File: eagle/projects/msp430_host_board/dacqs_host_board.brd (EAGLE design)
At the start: 127 x 100 mm, 272 parts, among them J1 MOL-SL-4-RA, J10 MOL-SL-3-V, J11 MOL-SL-2-V, J12 CONN HEADER 20POS .100" DBL, J13 MOL-SL-2-RA, J14 USB_MICROB_RECPT, J16 MOL-SL-2-RA, J17 CLM-112-02-L-D-IMU-MOUNT_IMU, J18 MOLSL-7-RA, J19 CONN HEADER 20POS .100" DBL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

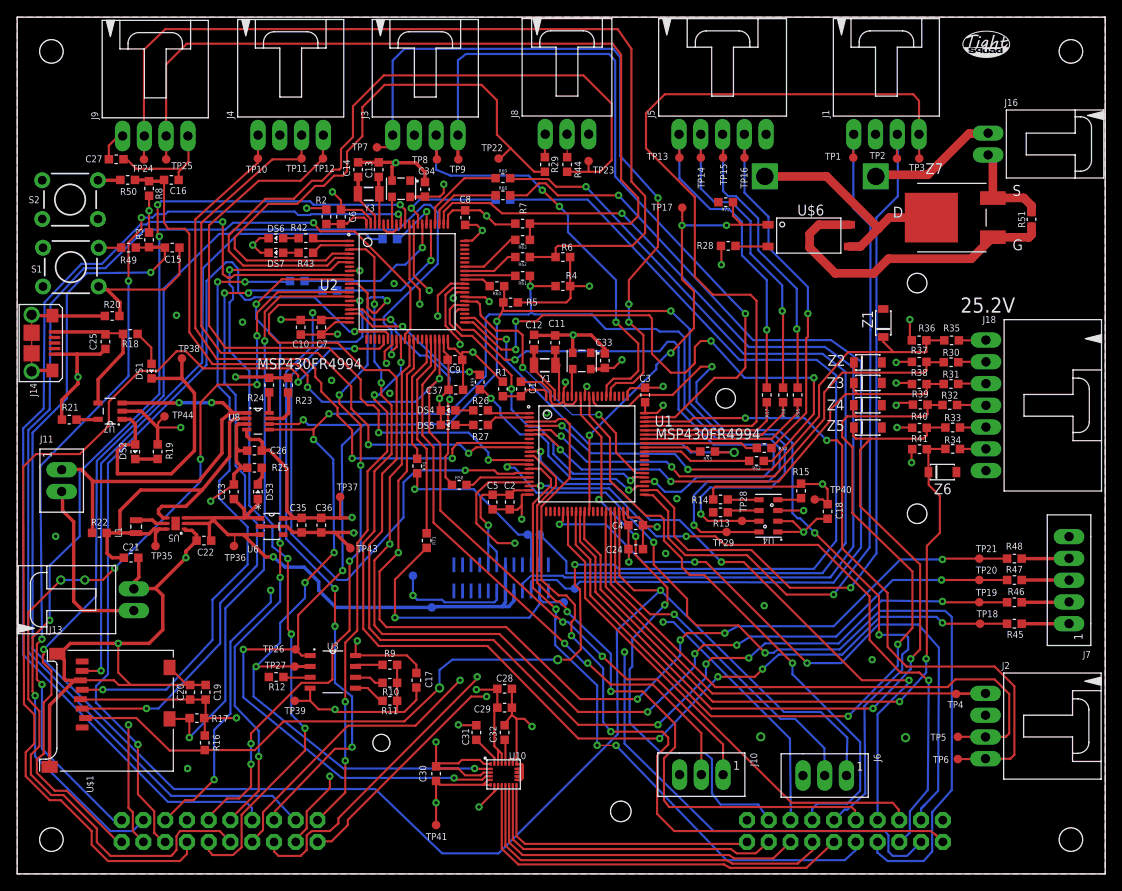
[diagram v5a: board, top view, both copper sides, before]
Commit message: Removed a large trace on power plane, updated some silkscreen
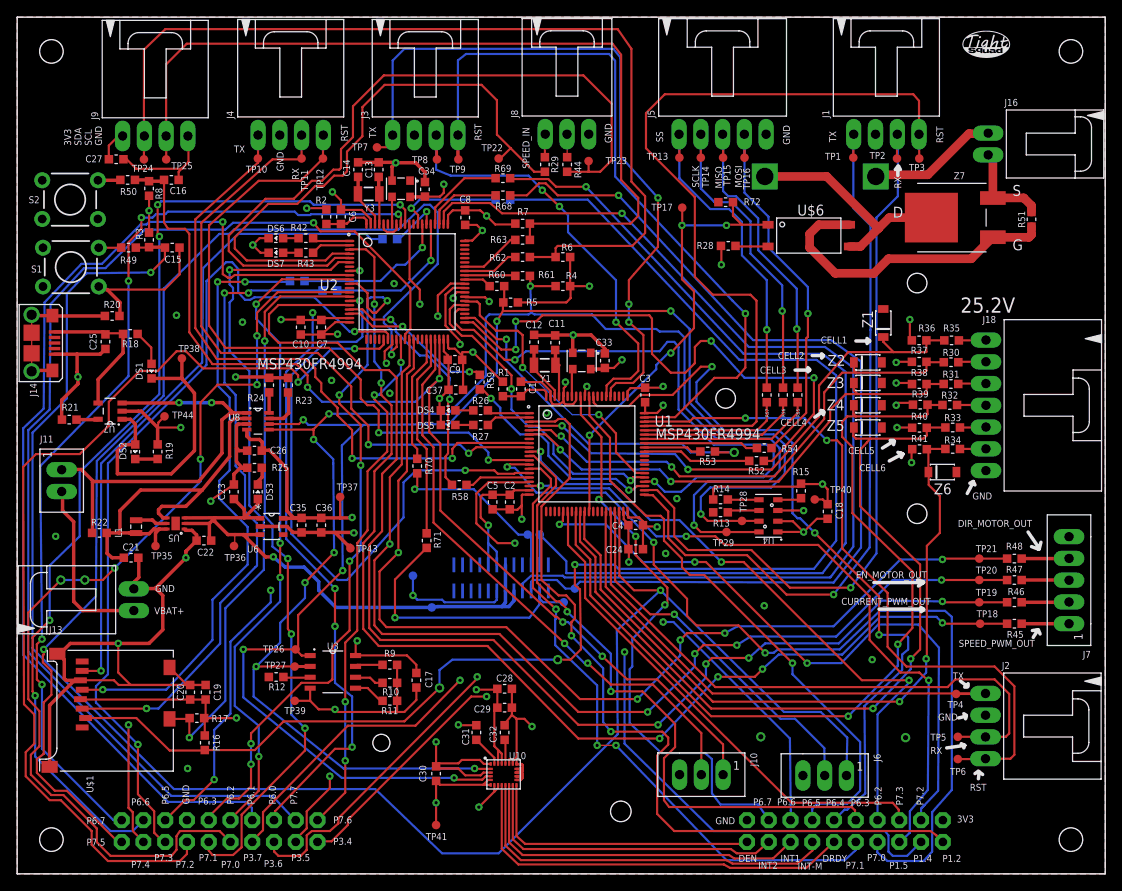
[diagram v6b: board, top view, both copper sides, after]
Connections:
- net GND: now also J19.14
- net P6.4_2: no longer J19.14
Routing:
- net P6.4_2: track 82.1 -> 0.00 mm, vias 1 -> 0
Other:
- board text added: "3V3"
- board text added: "CELL1"
- board text added: "CELL2"
- board text added: "CELL3"
- board text added: "CELL4"
- board text added: "CELL5"
- board text added: "CELL6"
- board text added: "CURRENT_PWM_OUT"
- board text added: "DEN"
- board text added: "DIR_MOTOR_OUT"
- board text added: "DRDY"
- board text added: "EN_MOTOR_OUT"
- board text added: "GND"
- board text added: "INT-M"
- board text added: "INT1"
- board text added: "INT2"
- board text added: "MISO"
- board text added: "MOSI"
- board text added: "P1.2"
- board text added: "P1.4"
- board text added: "P1.5"
- board text added: "P3.4"
- board text added: "P3.5"
- board text added: "P3.6"
- board text added: "P3.7"
- board text added: "P6.0"
- board text added: "P6.1"
- board text added: "P6.2"
- board text added: "P6.3"
- board text added: "P6.4"
- board text added: "P6.5"
- board text added: "P6.6"
- board text added: "P6.7"
- board text added: "P7.0"
- board text added: "P7.1"
- board text added: "P7.2"
- board text added: "P7.3"
- board text added: "P7.4"
- board text added: "P7.5"
- board text added: "P7.6"
- board text added: "P7.7"
- board text added: "RST"
- board text added: "RX"
- board text added: "SCL"
- board text added: "SCLK"
- board text added: "SDA"
- board text added: "SPEED_IN"
- board text added: "SPEED_PWM_OUT"
- board text added: "SS"
- board text added: "TX"
- board text added: "VBAT+"

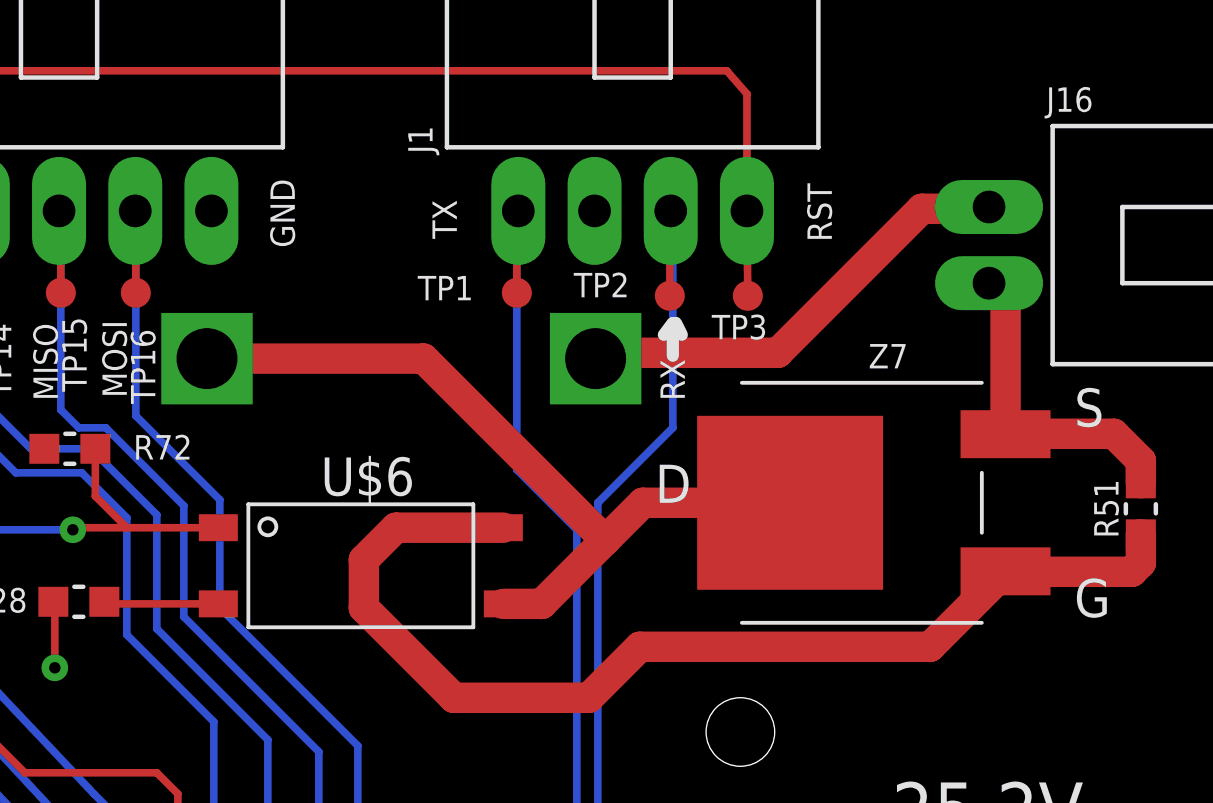
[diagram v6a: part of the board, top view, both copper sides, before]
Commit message: Made cutdown traces wider
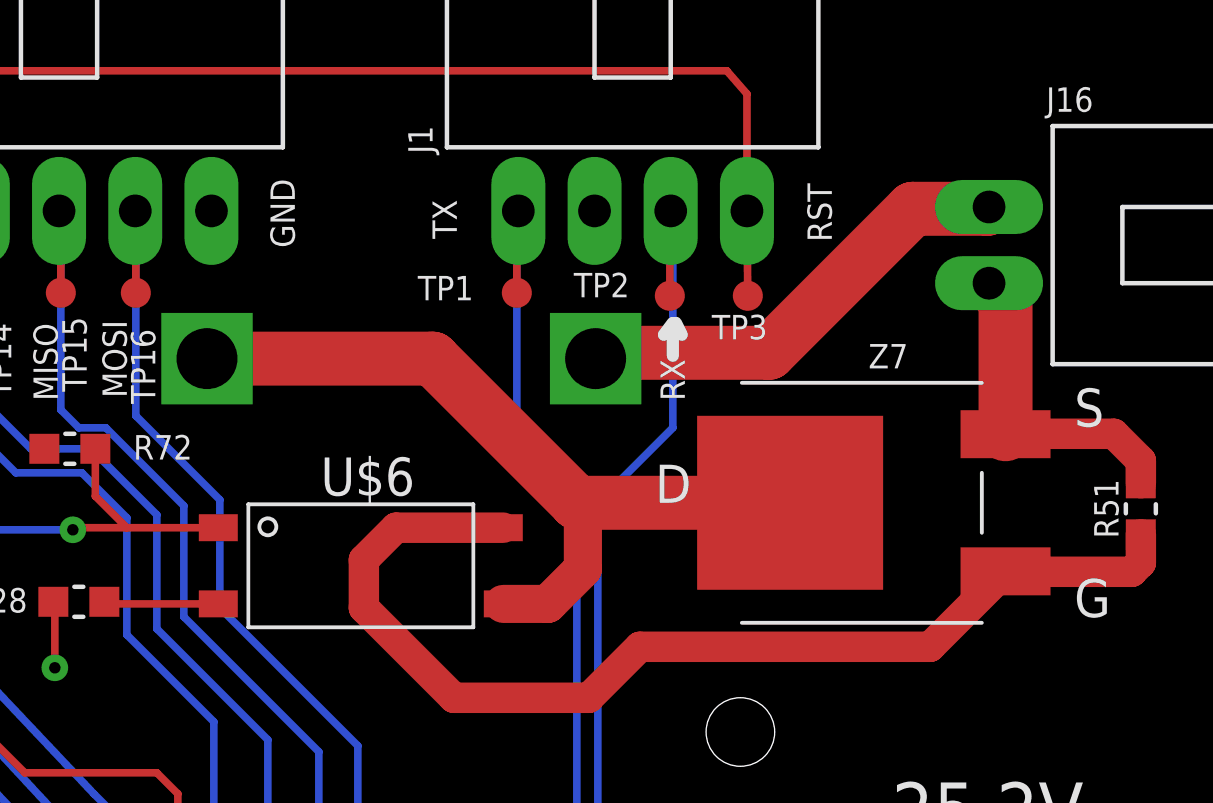
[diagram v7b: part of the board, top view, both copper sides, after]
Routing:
- net 9V_GND: track 26.7 -> 27.7 mm
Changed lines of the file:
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@@
 <contactref element="BAT1" pad="V+"/>
 <contactref element="J16" pad="1"/>
-<wire x1="113.28" y1="87.4" x2="113.34" y2="87.46" width="0.4064" layer="1"/>
-<wire x1="113.28" y1="87.4" x2="111.1" y2="87.4" width="1.016" layer="1"/>
-<wire x1="111.1" y1="87.4" x2="106.3" y2="82.6" width="1.016" layer="1"/>
-<wire x1="106.3" y1="82.6" x2="100.42" y2="82.6" width="1.016" layer="1"/>
 <wire x1="100.42" y1="82.6" x2="100.226" y2="82.406" width="1.016" layer="1"/>
+<wire x1="100.42" y1="82.6" x2="106" y2="82.6" width="1.8" layer="1"/>
+<wire x1="106" y1="82.6" x2="110.8" y2="87.4" width="1.8" layer="1"/>
+<wire x1="110.8" y1="87.4" x2="113.28" y2="87.4" width="1.8" layer="1"/>
+<wire x1="113.28" y1="87.4" x2="113.34" y2="87.46" width="1.8" layer="1"/>
 </signal>
 <signal name="CUTDOWN_DRAIN">
@@
 <wire x1="117.5" y1="79.9" x2="113.905" y2="79.9" width="1.016" layer="1"/>
 <wire x1="113.905" y1="79.9" x2="113.89" y2="79.885" width="1.016" layer="1"/>
-<wire x1="113.89" y1="79.885" x2="113.89" y2="84.37" width="1.016" layer="1"/>
-<wire x1="113.89" y1="84.37" x2="113.34" y2="84.92" width="1.016" layer="1"/>
+<wire x1="113.89" y1="79.885" x2="113.89" y2="84.37" width="1.8" layer="1"/>
+<wire x1="113.89" y1="84.37" x2="113.34" y2="84.92" width="1.8" layer="1"/>
 </signal>
 <signal name="TEMP_I2C_A0">
@@
 <contactref element="U$6" pad="P$3"/>
 <contactref element="Z7" pad="P$3"/>
-<wire x1="97.15" y1="74.23" x2="98.43" y2="74.23" width="1.016" layer="1"/>
-<wire x1="98.43" y1="74.23" x2="100.55" y2="76.35" width="1.016" layer="1"/>
-<wire x1="100.55" y1="76.35" x2="101.8" y2="77.6" width="1.016" layer="1"/>
-<wire x1="101.8" y1="77.6" x2="106.71" y2="77.6" width="1.016" layer="1"/>
-<wire x1="87.272" y1="82.406" x2="94.494" y2="82.406" width="1.016" layer="1"/>
-<wire x1="94.494" y1="82.406" x2="100.55" y2="76.35" width="1.016" layer="1"/>
+<wire x1="87.272" y1="82.406" x2="94.794" y2="82.406" width="1.8" layer="1"/>
+<wire x1="94.794" y1="82.406" x2="99.6" y2="77.6" width="1.8" layer="1"/>
+<wire x1="99.6" y1="77.6" x2="107.4" y2="77.6" width="1.8" layer="1"/>
+<wire x1="107.4" y1="77.6" x2="107.5" y2="77.7" width="1.8" layer="1"/>
+<wire x1="97.15" y1="74.23" x2="98.63" y2="74.23" width="1.27" layer="1"/>
+<wire x1="98.63" y1="74.23" x2="99.8" y2="75.4" width="1.27" layer="1"/>
+<wire x1="99.8" y1="75.4" x2="99.8" y2="77.4" width="1.27" layer="1"/>
+<wire x1="99.8" y1="77.4" x2="99.6" y2="77.6" width="1.27" layer="1"/>
+<wire x1="107.4" y1="77.6" x2="106.71" y2="77.6" width="0" layer="19" extent="1-1"/>
 </signal>
 <signal name="OPTO_OUT">
